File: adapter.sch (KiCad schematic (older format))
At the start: 15 parts, among them P1 CONN_02X05, P3 CONN_02X06, Q1 BSS138, U1 MC34063

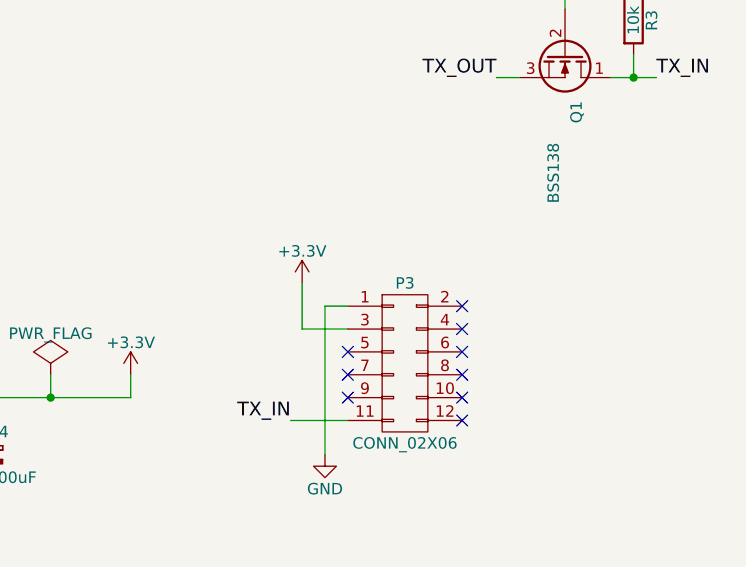
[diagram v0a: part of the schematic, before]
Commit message: Changed 2mm pitch array footpring a little.
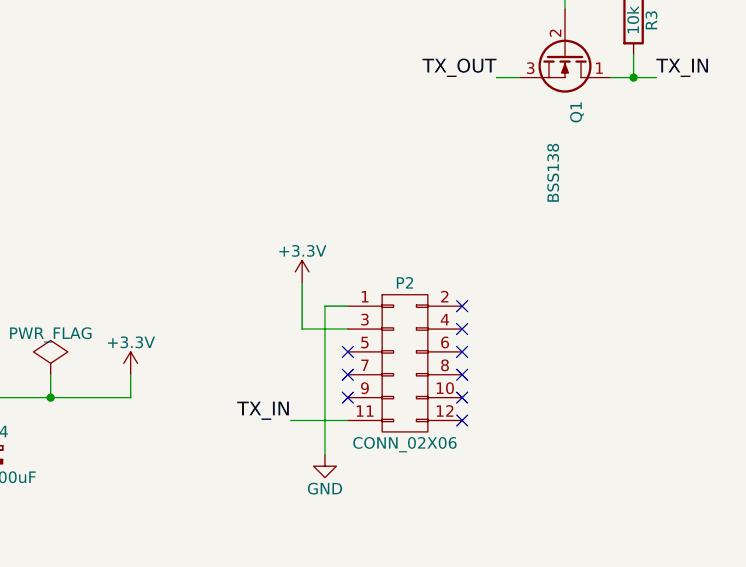
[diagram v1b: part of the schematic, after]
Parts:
- C4: footprint Capacitors_SMD:c_elec_6.3x5.7 -> Capacitors_SMD:c_elec_6.3x7.7
- L2: footprint Choke_SMD:Choke_SMD_1206_Handsoldering -> Capacitors_SMD:C_1210_HandSoldering
- Rsc1: footprint Resistors_ThroughHole:Resistor_Horizontal_RM10mm -> Resistors_ThroughHole:Resistor_Horizontal_RM15mm
- renumbered P3 to P2
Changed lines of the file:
@@
 F 0 "Rsc1" V 2380 2800 50  0000 C CNN
 F 1 "0.3R" V 2300 2800 50  0000 C CNN
-F 2 "Resistors_ThroughHole:Resistor_Horizontal_RM10mm" V 2230 2800 30  0001 C CNN
+F 2 "Resistors_ThroughHole:Resistor_Horizontal_RM15mm" V 2230 2800 30  0001 C CNN
 F 3 "" H 2300 2800 30  0000 C CNN
 	1    2300 2800
@@
 F 0 "L2" V 4700 4500 50  0000 C CNN
 F 1 "1uH" V 4850 4500 50  0000 C CNN
-F 2 "Choke_SMD:Choke_SMD_1206_Handsoldering" H 4750 4500 60  0001 C CNN
+F 2 "Capacitors_SMD:C_1210_HandSoldering" H 4750 4500 60  0001 C CNN
 F 3 "" H 4750 4500 60  0000 C CNN
 	1    4750 4500
@@
 F 0 "C4" H 5175 4850 50  0000 L CNN
 F 1 "100uF" H 5175 4650 50  0000 L CNN
-F 2 "Capacitors_SMD:c_elec_6.3x5.7" H 5188 4600 30  0001 C CNN
+F 2 "Capacitors_SMD:c_elec_6.3x7.7" H 5188 4600 30  0001 C CNN
 F 3 "" H 5150 4750 60  0000 C CNN
 	1    5150 4750
@@
 $EndComp
 $Comp
-L CONN_02X06 P3
+L CONN_02X06 P2
 U 1 1 559EAA41
 P 7000 4350
-F 0 "P3" H 7000 4700 50  0000 C CNN
+F 0 "P2" H 7000 4700 50  0000 C CNN
 F 1 "CONN_02X06" H 7000 4000 50  0000 C CNN
 F 2 "DSMX Tx module adapter:Socket_Strip_Straight_2x06_pitch2mm" H 7000 3150 60  0001 C CNN
